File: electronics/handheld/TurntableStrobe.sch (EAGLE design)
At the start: 18 parts, among them IC1 TINY25, J1 ISP, Q1 12MHz

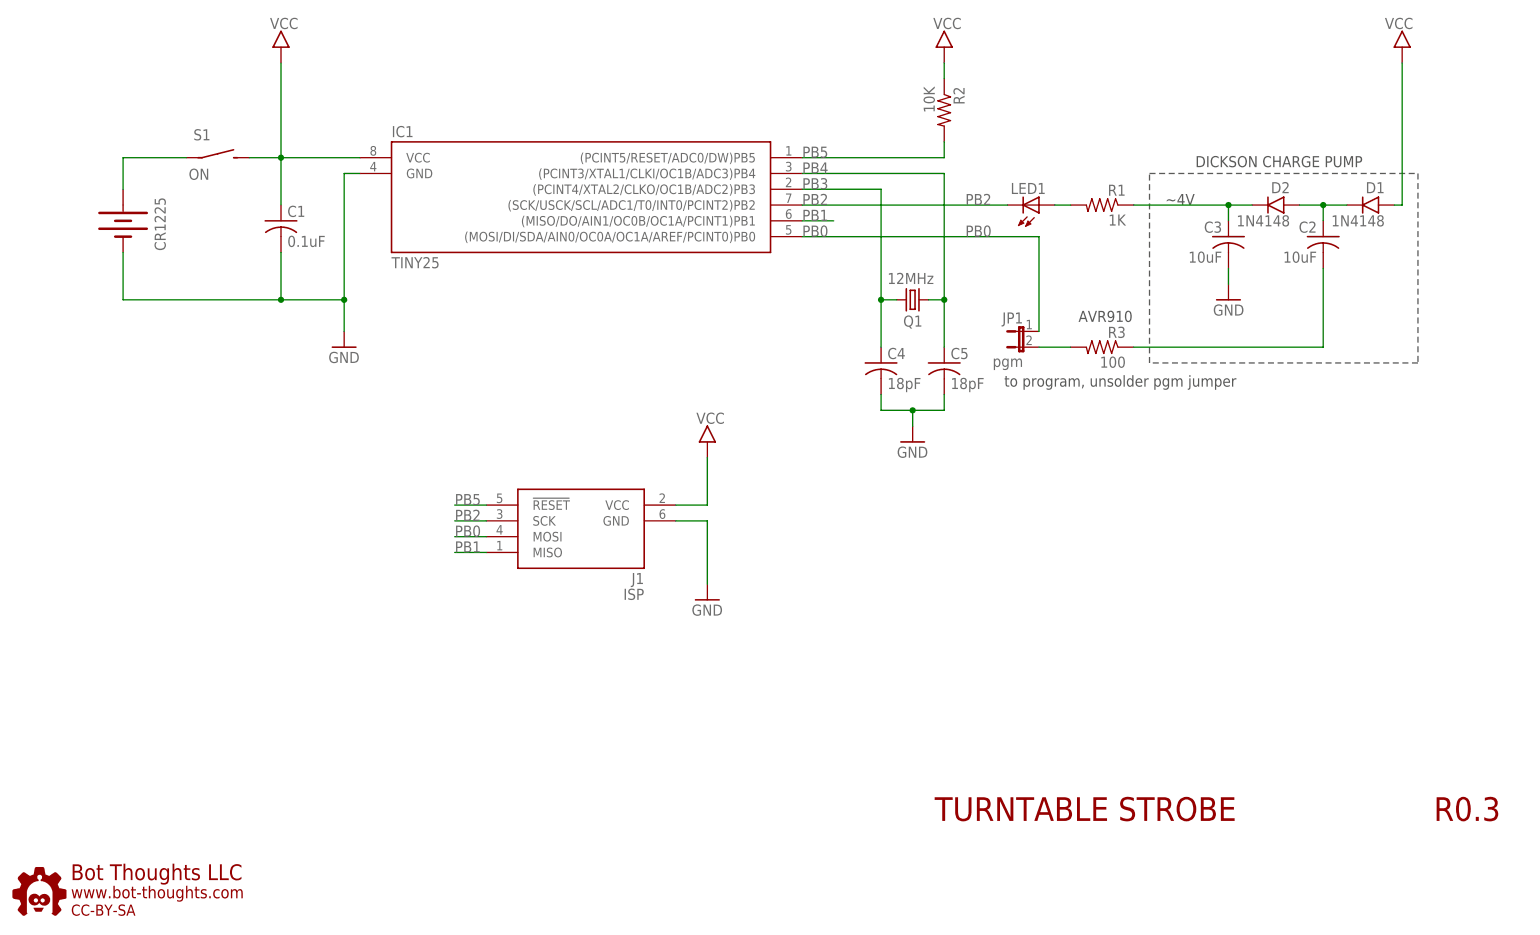
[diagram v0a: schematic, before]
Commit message: Prototype LM2665 charge pump
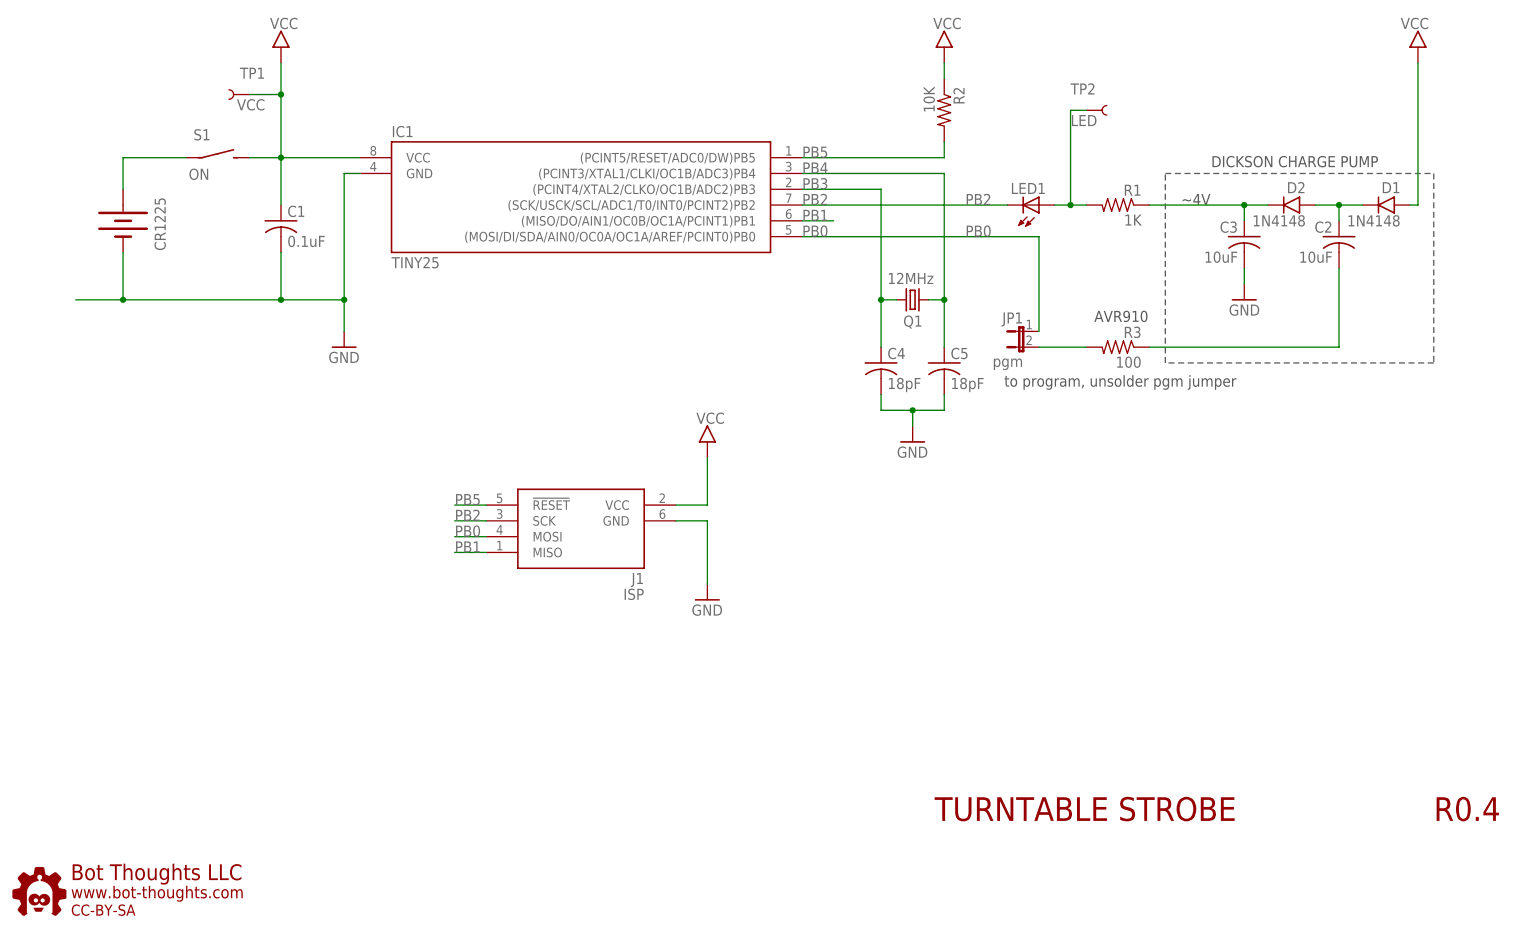
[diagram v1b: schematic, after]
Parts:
- added TP1: VCC, SparkFun-Connectors:TEST-POINT3X5
- added TP2: LED, SparkFun-Connectors:TEST-POINT3X5
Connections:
- net N$3: now also TP2.1
- net VCC: now also TP1.1
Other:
- note added: "R0.4"
- note removed: "R0.3"
- moved on the sheet: C2, C3, D1, D2, R1, R3
